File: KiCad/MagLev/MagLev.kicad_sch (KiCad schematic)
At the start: 72 parts, among them J1 Barrel_Jack, Q12 AOD442G, Q13 AOD442G, Q17 ZX5T851GTA, Q18 ZX5T1951GTA, Q5 ZX5T1951GTA, U10 X, U11 Y, U12 Z, U13 MCP1402, U14 MCP1402, U3 L78L05_SO8, U4 TL431A, U5 LM393, X1 L_Ferrite, X2 L_Ferrite, Y1 L_Ferrite, Y2 L_Ferrite, Y5 L_Ferrite, Y6 L_Ferrite, Y8 L_Ferrite, Y9 L_Ferrite

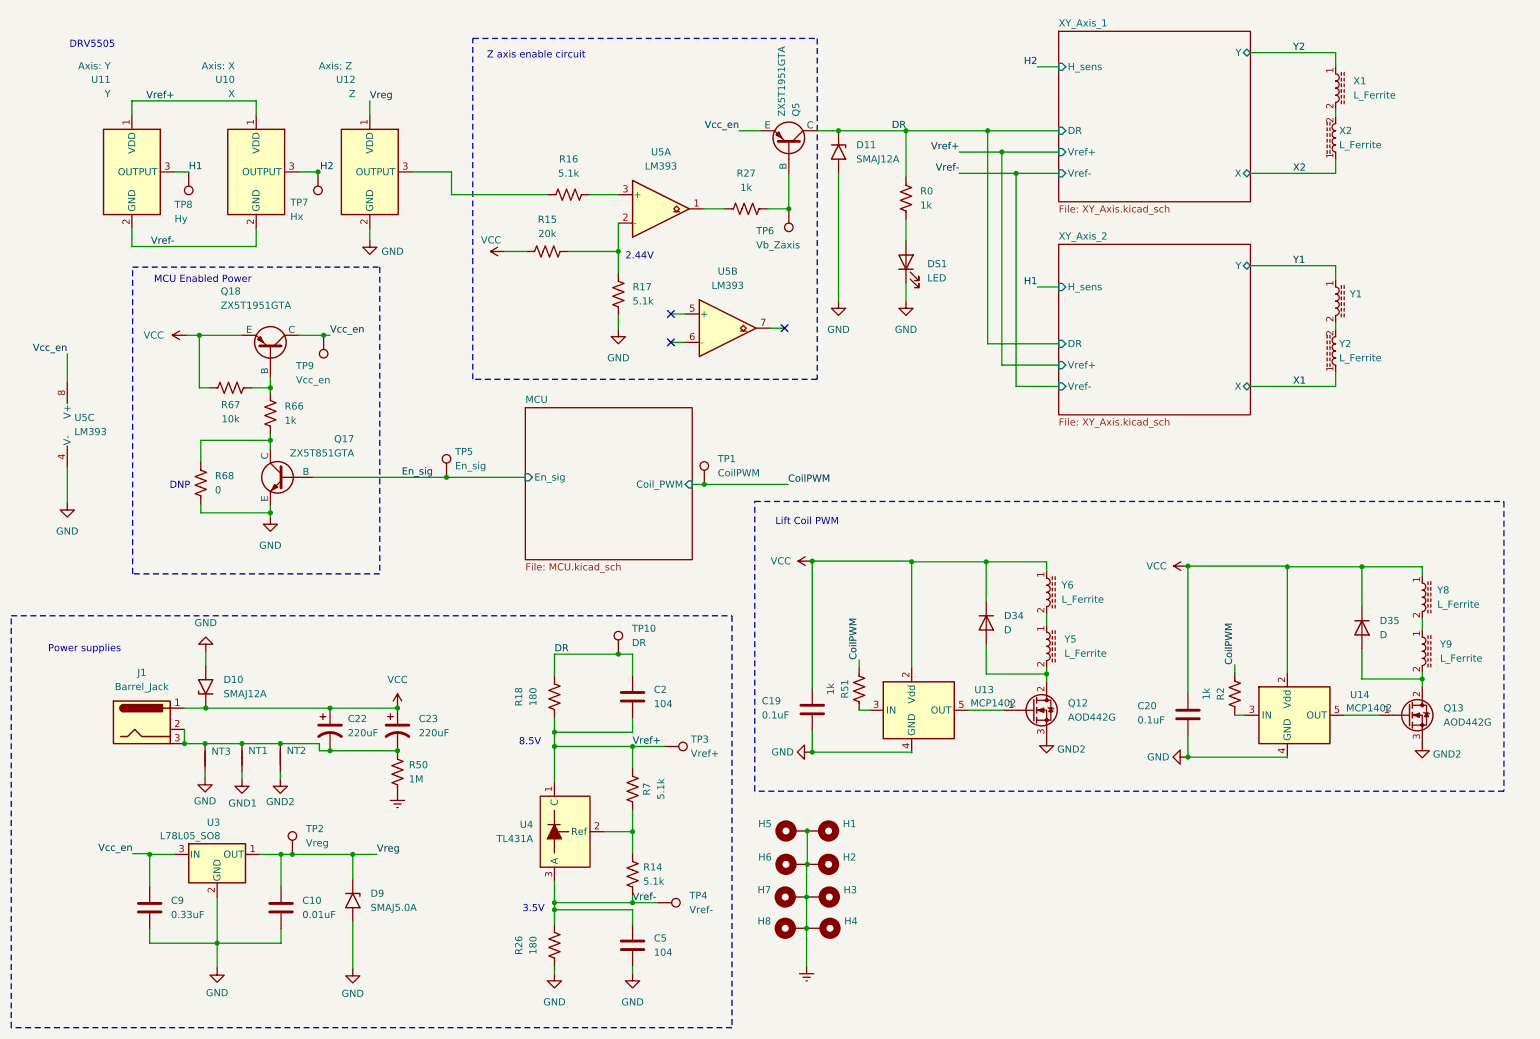
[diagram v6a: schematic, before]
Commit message: Finish layout up to TPs.
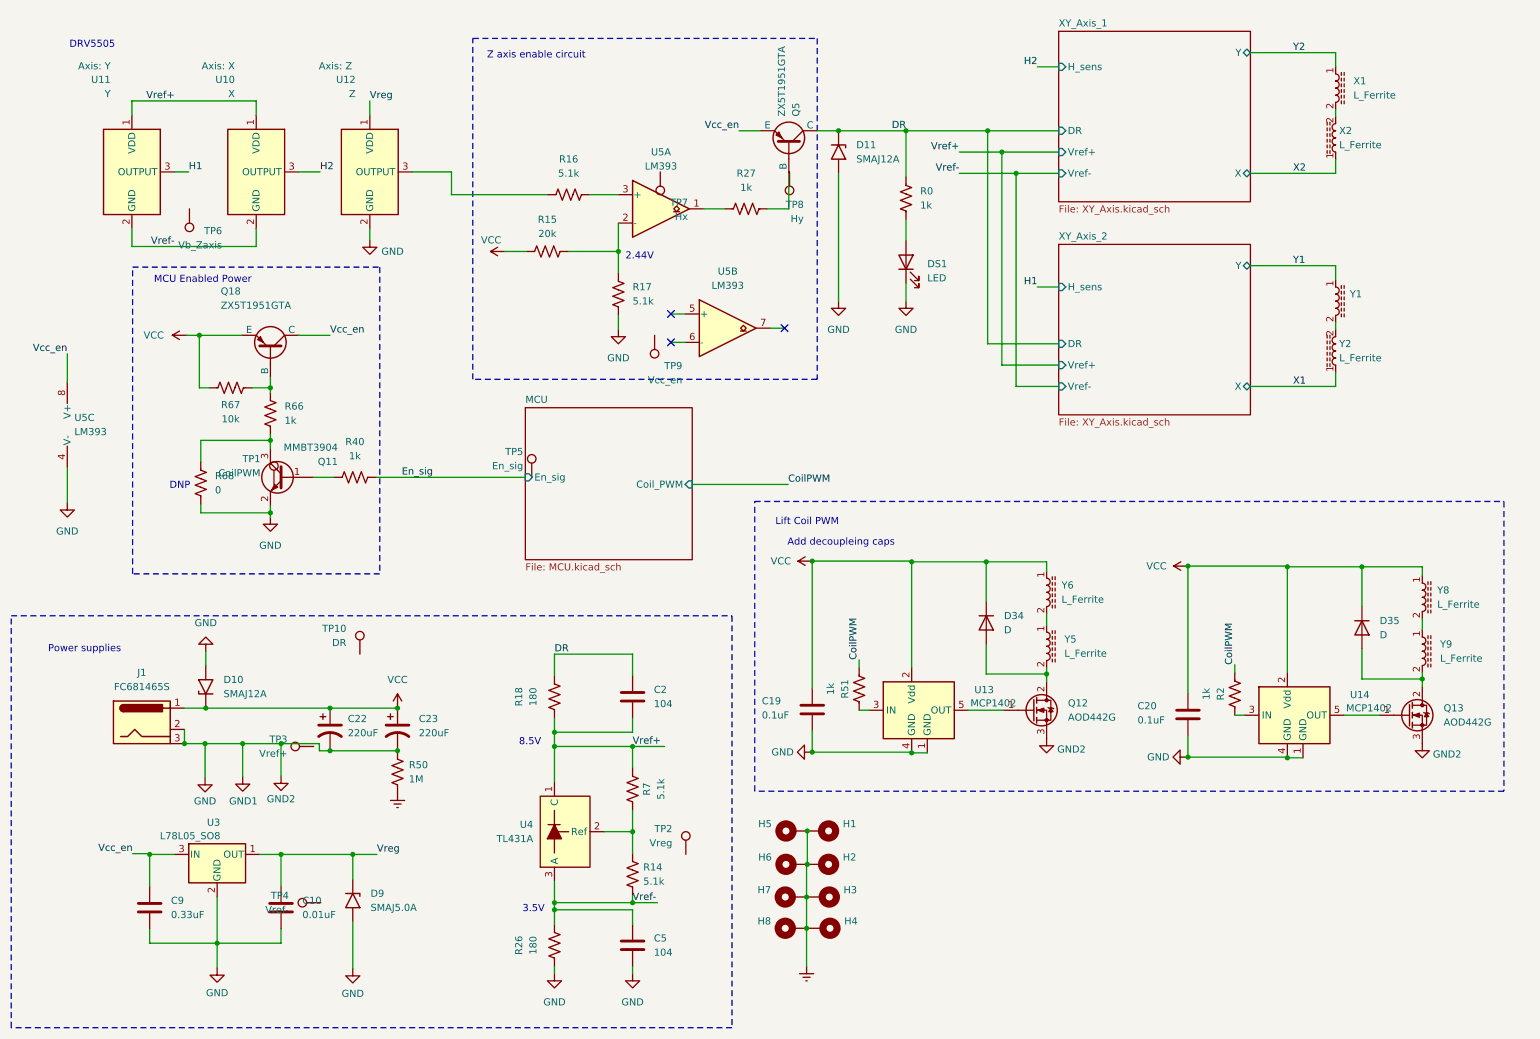
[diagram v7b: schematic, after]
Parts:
- removed NT1, NT2: NetTie_2, NetTie:NetTie-2_SMD_Pad2.0mm, symbol Device:NetTie_2
- removed NT3: NetTie_2, NetTie:NetTie-2_SMD_Pad0.5mm, symbol Device:NetTie_2
- removed Q17: ZX5T851GTA, Maglev_Footprint_Library:SOT-223-3_TabPin2_BJT, symbol Simulation_SPICE:NPN
- added Q11: MMBT3904, Package_TO_SOT_SMD:SOT-23, symbol Transistor_BJT:MMBT3904
- added R40: 1k, Resistor_SMD:R_0805_2012Metric_Pad1.20x1.40mm_HandSolder, symbol Device:R_US
- J1: value Barrel_Jack -> FC681465S; footprint Connector_BarrelJack:BarrelJack_Horizontal -> Maglev_Footprint_Library:BarrelJack_CLIFF_FC681465S_SMT_Horizontal_No_Holes
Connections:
- net GND2 is gone; now on net GND: Q12.3 (S), Q13.3 (S)
- net CoilPWM: no longer TP1.1
- net DR: no longer TP10.1
- net En_sig: now also R40.2; no longer TP5.1
- net GND: now also C22.2, C23.2, J1.2, J1.3, R50.1, U13.1 (NC), U14.1 (NC), Q11.2 (E)
- net H1: no longer TP8.1
- net H2: no longer TP7.1
- net Vcc_en: no longer TP9.1
- net Vref+: no longer TP3.1
- net Vref-: no longer TP4.1
- net Vreg: no longer TP2.1
- net at Q5.2 (B), R27.2: no longer TP6.1
- net at R66.2, R68.1: now also Q11.3 (C)
- new net: Q11.1 (B), R40.1
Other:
- note added: "Add decoupleing caps"
- moved on the sheet: TP1, TP10, TP2, TP3, TP4, TP5, TP6, TP7, TP8, TP9

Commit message: Route TPs, increase power trace size.
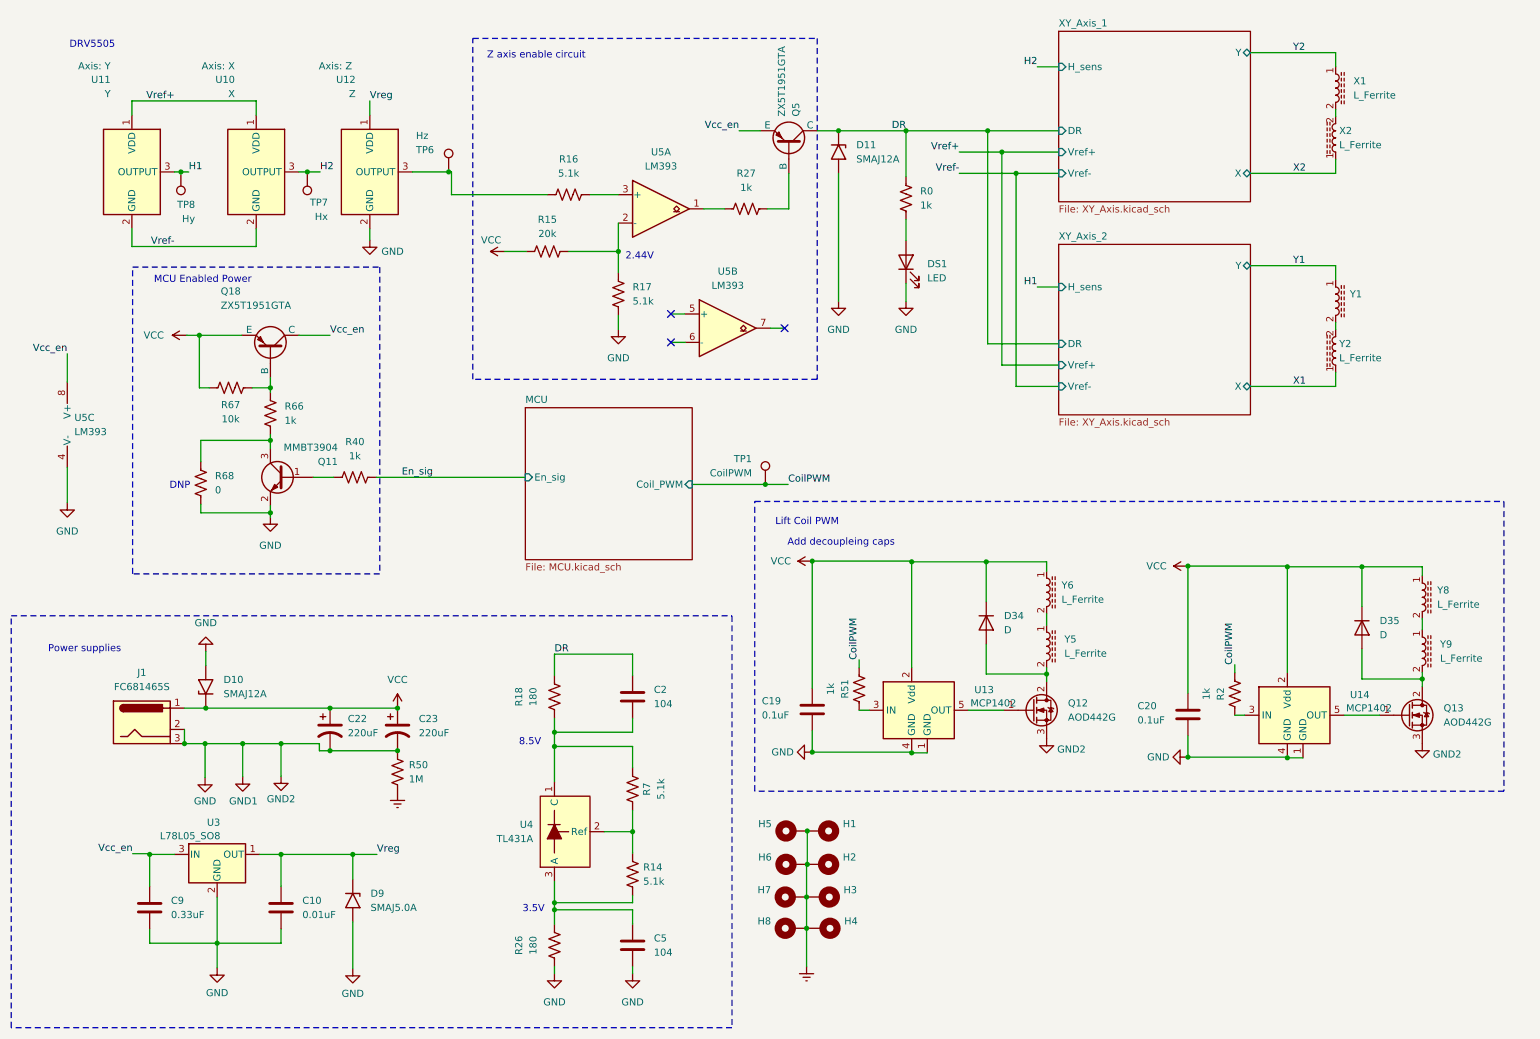
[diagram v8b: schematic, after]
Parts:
- removed TP10: DR, TestPoint:TestPoint_Pad_D2.0mm, symbol Connector:TestPoint
- removed TP2: Vreg, TestPoint:TestPoint_Pad_D2.0mm, symbol Connector:TestPoint
- removed TP3: Vref+, TestPoint:TestPoint_Pad_D2.0mm, symbol Connector:TestPoint
- removed TP4: Vref-, TestPoint:TestPoint_Pad_D2.0mm, symbol Connector:TestPoint
- removed TP5: En_sig, TestPoint:TestPoint_Pad_D2.0mm, symbol Connector:TestPoint
- removed TP9: Vcc_en, TestPoint:TestPoint_Pad_D2.0mm, symbol Connector:TestPoint
- TP6: value Vb_Zaxis -> Hz
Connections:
- net CoilPWM: now also TP1.1
- net H1: now also TP8.1
- net H2: now also TP7.1
- net Vref+: no longer C2.2, R18.1, R7.2, U4.1 (C)
- net Vref-: no longer C5.1, R14.2, R26.2, U4.3 (A)
- net at R16.2, U12.3 (OUTPUT): now also TP6.1
- new net: C2.2, R18.1, R7.2, U4.1 (C)
- new net: C5.1, R14.2, R26.2, U4.3 (A)
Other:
- moved on the sheet: TP1, TP6, TP7, TP8
